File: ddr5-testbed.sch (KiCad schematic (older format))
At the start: 2 parts

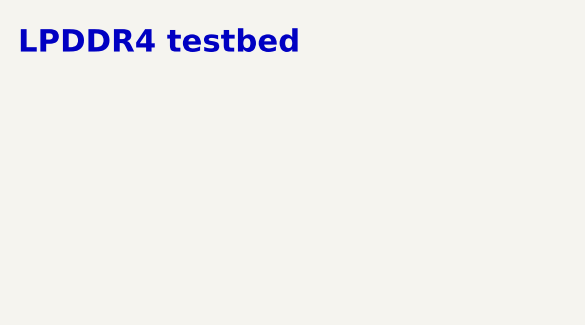
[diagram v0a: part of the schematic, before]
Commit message: Update project name on schematic
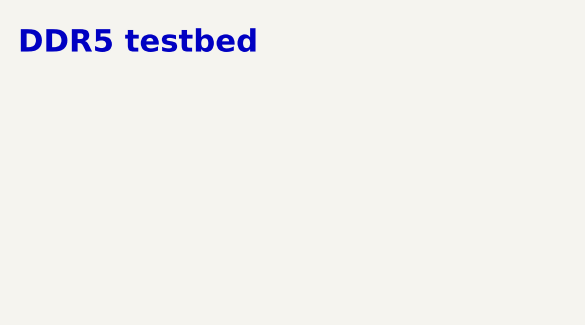
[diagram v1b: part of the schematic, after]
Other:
- note added: "DDR5 testbed"
- note removed: "LPDDR4 testbed"
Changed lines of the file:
@@
 $EndSheet
 Text Notes 725  850  0    98   ~ 20
-LPDDR4 testbed
+DDR5 testbed
 $Sheet
 S 8625 5250 1650 1125
